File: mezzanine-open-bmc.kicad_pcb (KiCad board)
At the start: 2 copper layers, 85 x 54 mm, 64 parts, among them P1 CONN_02X20, P2 CONN_02X20, P3 CONN_01X04, P4 CONN_01X04, P5 CONN_01X04, SW1 PWR, SW2 RST, U1 FT230XS, U2 PMIC-CJT1117-3.3(SOT223), U3 DS3231N, U4 PCA9306, U5 M24C16-WMN6P, U6 REG_1.8V, U7 PCA9306, U8 PCA9306

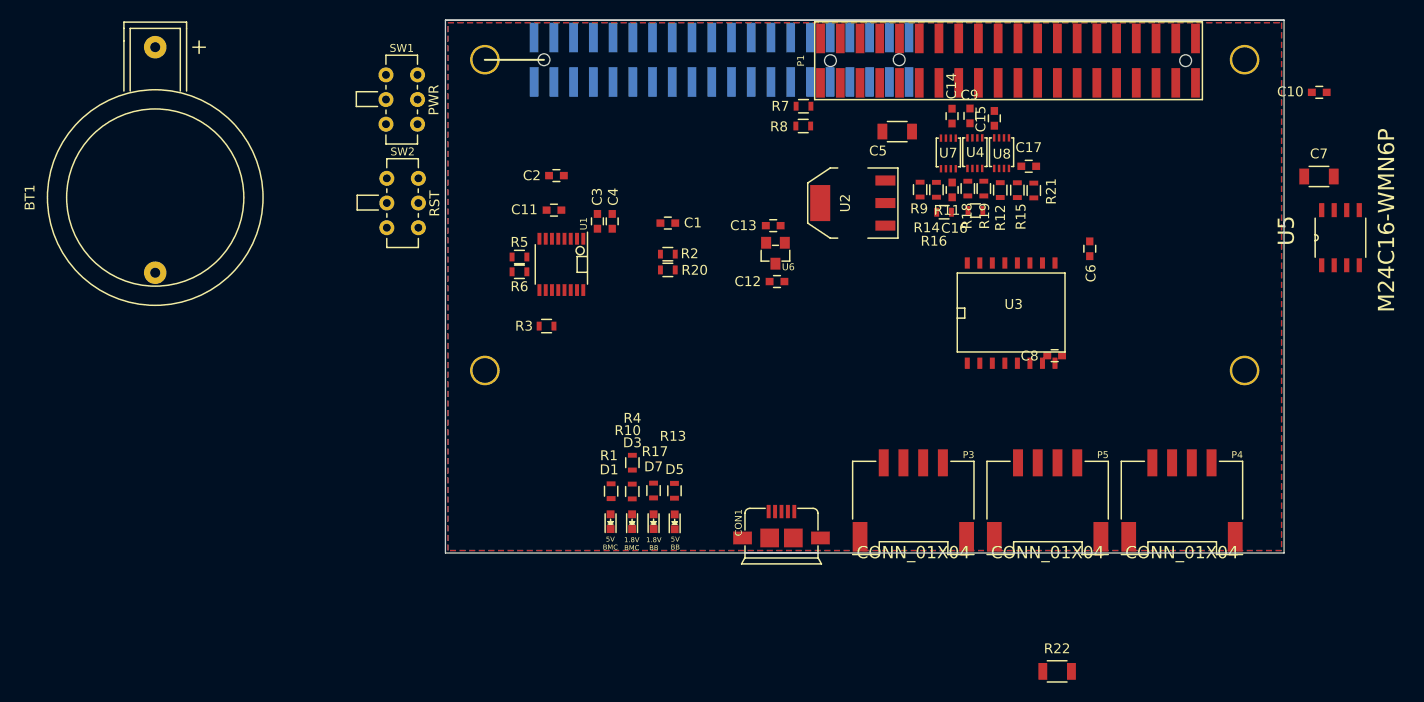
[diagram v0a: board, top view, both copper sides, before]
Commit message: Position USB and Connect
The USB is now positioned and all its important components are connected.

Signed-off-by: Sophie Haynes <sophie.haynes@linaro.org>
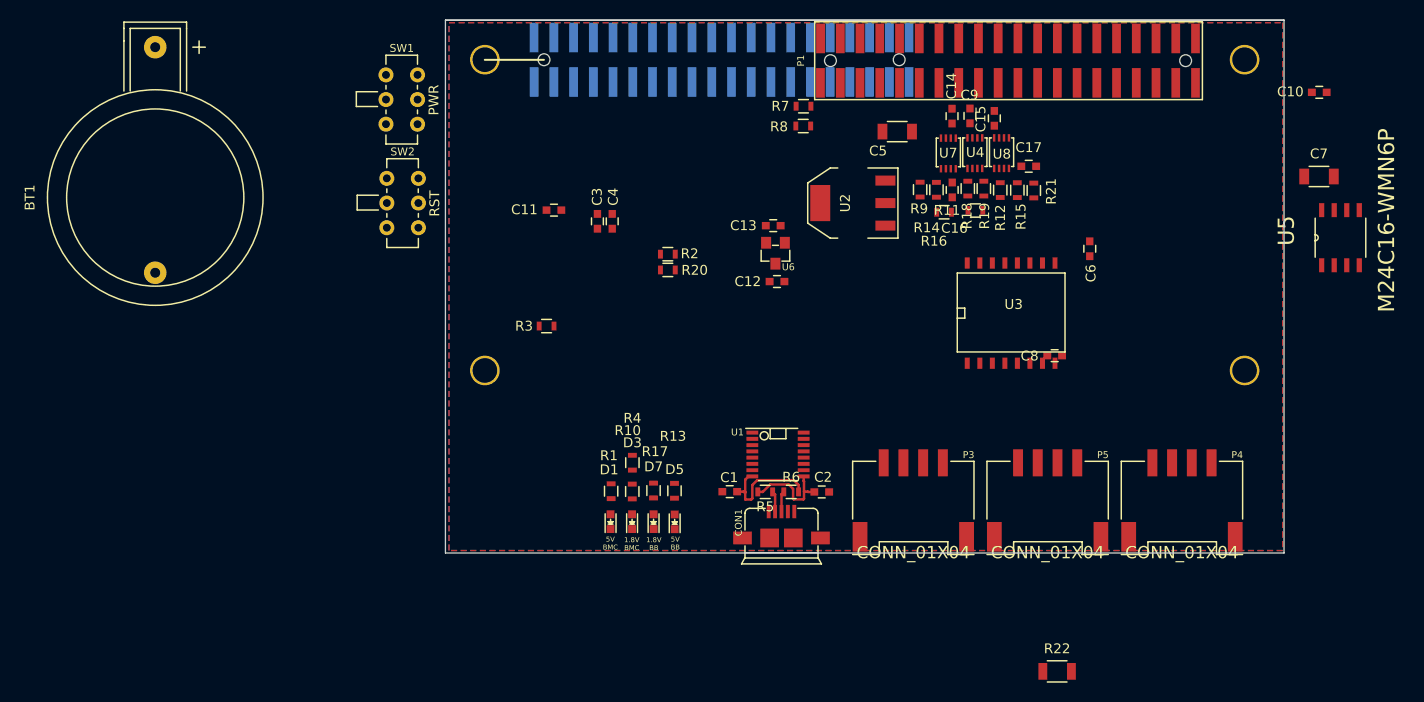
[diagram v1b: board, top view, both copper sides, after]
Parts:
- moved C2 41.8 mm to (138.1, 147.8)
- moved R6 35.4 mm to (135.0, 147.8), turned to 180 degrees
- moved R5 34.5 mm to (132.4, 147.8), turned to 0 degrees
- moved U1 29.2 mm to (133.7, 144.0), turned to 0 degrees
- moved C1 27.9 mm to (128.8, 147.8)
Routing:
- net /USB+: track 0.00 -> 13.7 mm
- net /USB-: track 0.00 -> 11.7 mm

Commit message: Move Switches to Bottom of Board
Signed-off-by: Sophie Haynes <sophie.haynes@linaro.org>
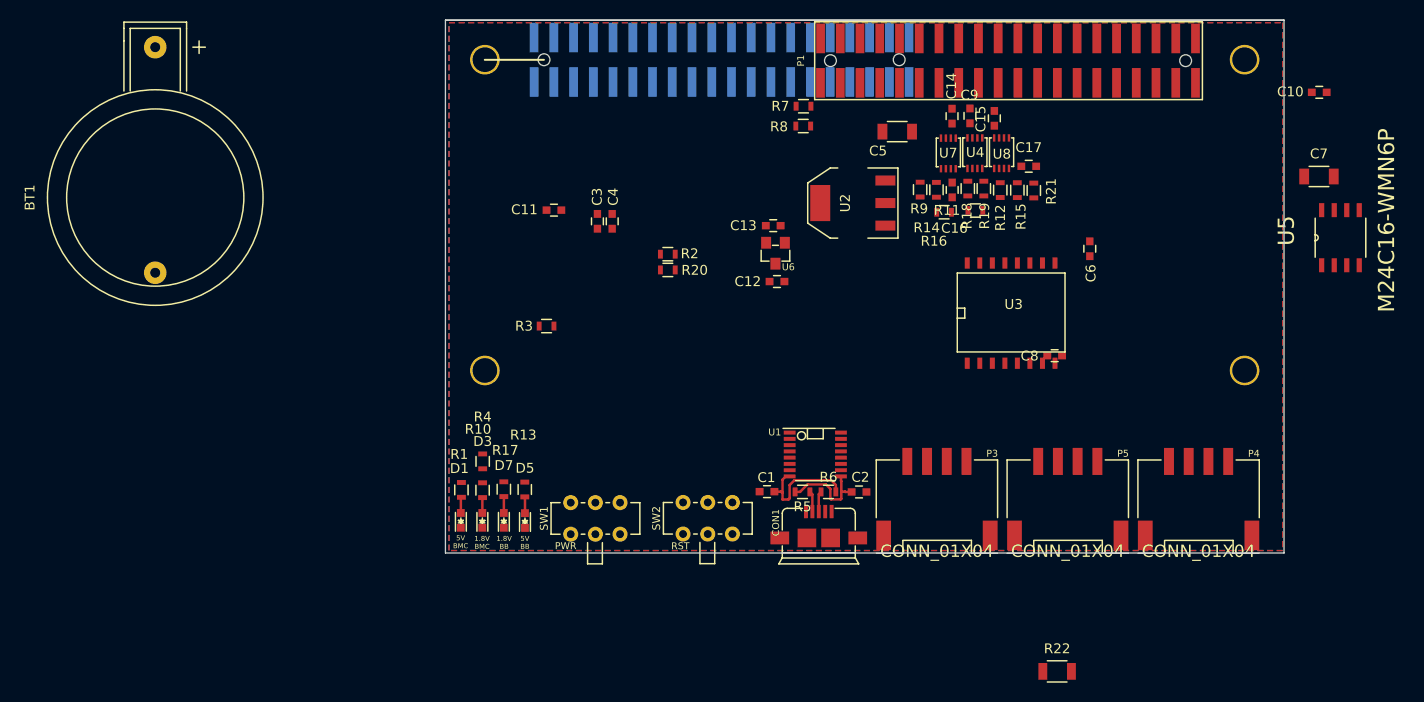
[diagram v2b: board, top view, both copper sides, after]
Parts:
- moved SW1 48.9 mm to (115.2, 152.1), turned to 0 degrees
- moved SW2 46.7 mm to (126.6, 152.1), turned to 0 degrees
- moved D3 15.2 mm to (103.7, 150.7)
- moved D7 15.2 mm to (105.9, 150.7)
- moved R13 15.2 mm to (108.0, 147.6)
- moved D1 15.2 mm to (101.6, 150.7)
- moved D5 15.2 mm to (108.1, 150.7)
- moved R1 15.2 mm to (101.6, 147.6)
- moved R10 15.2 mm to (103.8, 147.6)
- moved R17 15.2 mm to (105.9, 147.5)
- moved R4 15.2 mm to (103.8, 144.7)
- moved C1 3.78 mm to (132.6, 147.8)
- moved C2 3.78 mm to (141.9, 147.8)
- moved CON1 3.78 mm to (137.8, 154.0)
- moved R5 3.78 mm to (136.2, 147.8)
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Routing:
- net Net-(D7-Pad2): track 0.00 -> 1.66 mm
- net Net-(D5-Pad2): track 0.00 -> 1.65 mm
- net Net-(D1-Pad2): track 0.00 -> 1.61 mm
- net Net-(D3-Pad2): track 0.00 -> 1.57 mm

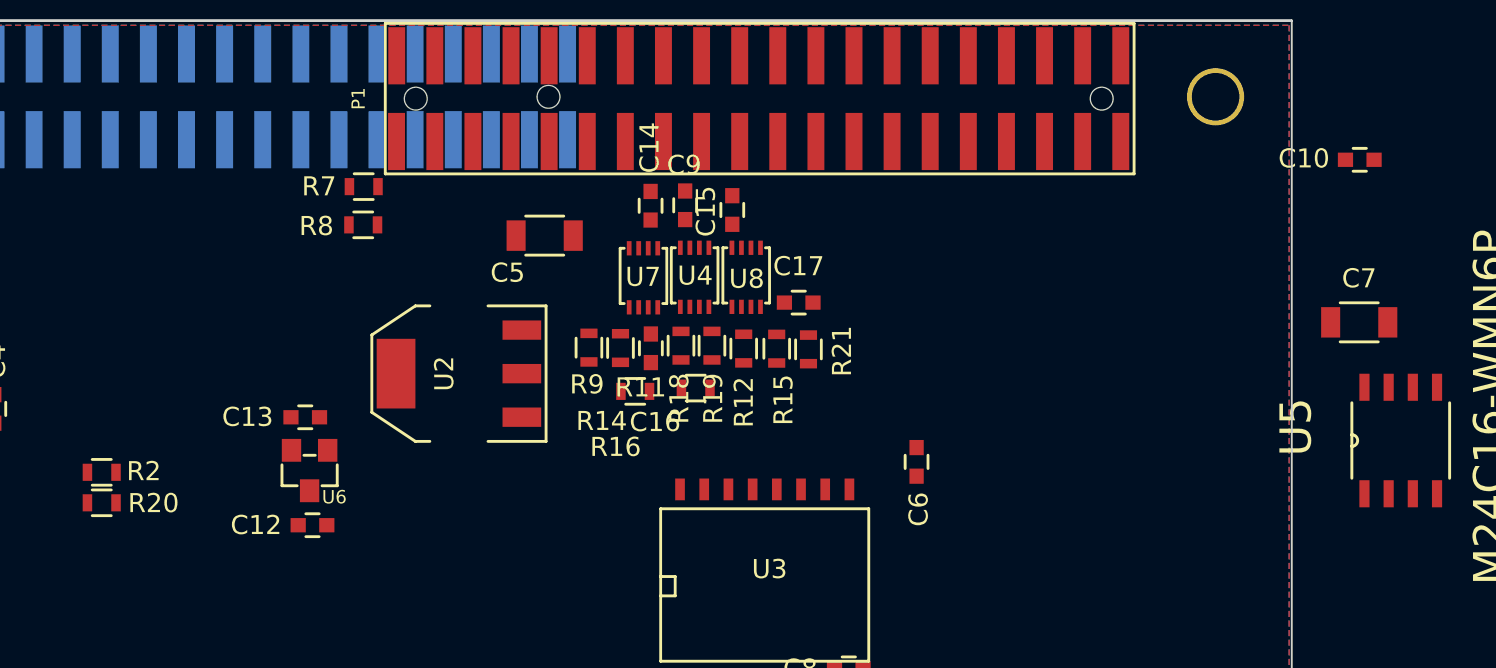
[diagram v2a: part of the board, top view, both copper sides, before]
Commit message: Position Grove Conn. Level Shifters
All three LS for the grove Connecotrs have been placed in a nice
layout in suitable location on board.

Signed-off-by: Sophie Haynes <sophie.haynes@linaro.org>
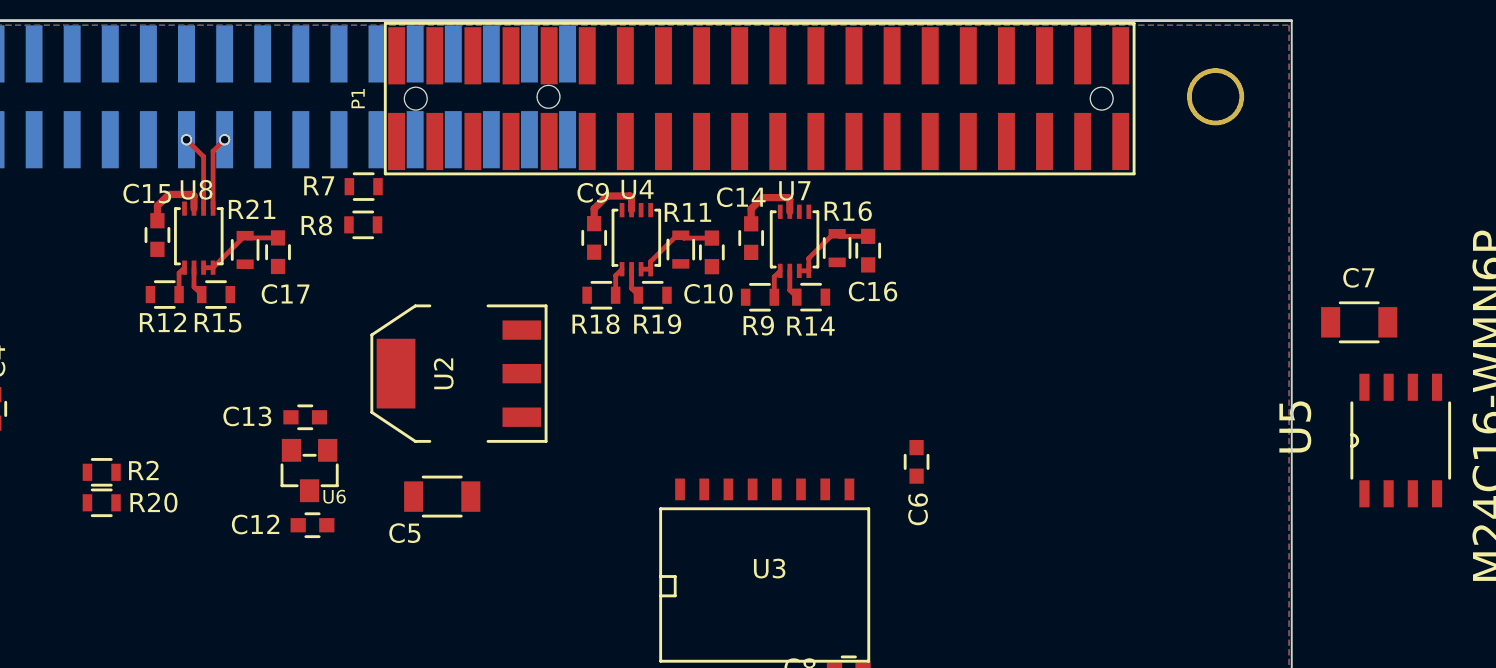
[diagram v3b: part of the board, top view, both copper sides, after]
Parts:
- moved C10 34.3 mm to (154.6, 112.2), turned to 270 degrees
- moved R12 30.5 mm to (125.9, 114.4), turned to 0 degrees
- moved C15 30.2 mm to (125.5, 111.3), turned to 270 degrees
- moved R21 30.0 mm to (130.1, 112.0)
- moved R15 29.6 mm to (128.5, 114.4), turned to 180 degrees
- moved U8 28.8 mm to (126.9, 109.9)
- moved C17 27.5 mm to (131.8, 112.2), turned to 270 degrees
- moved C5 14.7 mm to (140.4, 125.0)
- moved R16 13.0 mm to (161.1, 111.9), turned to 90 degrees
- moved C16 12.5 mm to (162.8, 112.1)
- moved R14 10.4 mm to (159.8, 114.5), turned to 180 degrees
- moved R9 9.36 mm to (157.1, 114.5), turned to 0 degrees
- moved U7 8.16 mm to (158.2, 110.0)
- moved R11 7.31 mm to (152.9, 112.0), turned to 90 degrees
- moved C14 5.54 mm to (156.6, 111.4), turned to 270 degrees
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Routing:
- net +1V8: track 0.00 -> 11.1 mm
- net Net-(C16-Pad1): track 0.00 -> 4.86 mm
- net Net-(C10-Pad1): track 0.00 -> 4.75 mm
- net Net-(C17-Pad1): track 0.00 -> 4.65 mm
- net I2C1_SDA: track 0.00 -> 4.06 mm, vias 0 -> 1
- net I2C1_SCL: track 0.00 -> 3.99 mm, vias 0 -> 1
- net I2C0_SCL_3.3: track 0.00 -> 1.72 mm
- net I2C1_SCL_3.3: track 0.00 -> 1.58 mm
- net I2C1_SCL_BMC_3.3: track 0.00 -> 1.53 mm
- net I2C1_SDA_3.3: track 0.00 -> 1.53 mm
- net I2C1_SDA_BMC_3.3: track 0.00 -> 1.52 mm
- net I2C0_SDA_3.3: track 0.00 -> 1.50 mm

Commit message: [WIP] PCB In Progress
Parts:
- U2: value PMIC-CJT1117-3.3(SOT223) -> SOT223
- moved R22 56.2 mm to (166.2, 110.0), turned to 180 degrees
- moved BT1 41.1 mm to (111.7, 119.5), turned to 270 degrees
- moved C11 38.0 mm to (142.4, 140.6), turned to 0 degrees
- moved C3 35.8 mm to (142.4, 143.8), turned to 0 degrees
- moved C5 34.5 mm to (171.5, 109.9)
- moved U3 33.8 mm to (123.8, 134.5), turned to 90 degrees
- moved C4 33.6 mm to (142.4, 142.3), turned to 0 degrees
- moved C8 31.2 mm to (130.7, 137.0), turned to 90 degrees
- moved U5 29.8 mm to (164.5, 136.3), turned to 0 degrees
- moved C7 27.3 mm to (165.8, 130.9), turned to 180 degrees
- moved U2 26.6 mm to (167.3, 124.0), turned to 0 degrees
- moved R3 25.1 mm to (132.5, 142.8)
- moved P4 25.0 mm to (151.3, 144.8)
- moved R2 24.5 mm to (132.4, 146.1), turned to 0 degrees
- moved R20 21.6 mm to (132.5, 144.5), turned to 0 degrees
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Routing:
- net +3V3: track 0.00 -> 96.0 mm
- net UART1_TX_BMC: track 0.00 -> 50.9 mm
- net UART1_RX_BMC: track 0.00 -> 48.0 mm
- net +1V8: track 11.1 -> 58.4 mm, vias 0 -> 2
- net GPIO_A: track 0.00 -> 41.9 mm, vias 0 -> 1
- net I2C0_SCL: track 0.00 -> 41.6 mm, vias 0 -> 1
- net I2C0_SDA: track 0.00 -> 40.1 mm, vias 0 -> 1
- net I2C1_SCL_BMC_3.3: track 1.53 -> 41.2 mm, vias 0 -> 2
- net I2C0_SDA_3.3: track 1.50 -> 40.7 mm, vias 0 -> 2
- net I2C1_SDA_BMC_3.3: track 1.52 -> 40.4 mm, vias 0 -> 2
- net I2C0_SCL_3.3: track 1.72 -> 40.5 mm, vias 0 -> 2
- net GPIO_B: track 0.00 -> 38.4 mm, vias 0 -> 1
- net GPIO_C_BMC: track 0.00 -> 37.4 mm, vias 0 -> 2
- net +5V: track 0.00 -> 35.3 mm
- net PWR_BTN_N: track 0.00 -> 30.5 mm, vias 0 -> 1
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
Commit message: [WIP]
Updating the repository, still drawing traces.

Signed-off-by: Sophie Haynes <sophie.haynes@linaro.org>
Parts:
- moved R22 9.64 mm to (160.6, 117.8)
- moved C5 3.03 mm to (174.4, 109.5), turned to 0 degrees
- moved R12 2.47 mm to (128.5, 116.1), turned to 180 degrees
- moved C10 2.08 mm to (155.1, 114.2)
- moved R11 2.08 mm to (153.5, 114.0)
- moved C17 2.06 mm to (132.4, 114.1)
- moved R21 2.06 mm to (130.6, 114.0)
- moved C9 2.01 mm to (147.8, 109.5), turned to 180 degrees
- moved R16 1.97 mm to (161.8, 113.8)
- moved C16 1.97 mm to (163.4, 113.9)
- moved R15 1.67 mm to (128.4, 114.5)
- moved C6 1.57 mm to (173.8, 112.0), turned to 0 degrees
- moved C14 1.57 mm to (156.6, 109.8)
- moved R7 0.96 mm to (135.0, 109.3)
- moved R8 0.96 mm to (137.1, 109.4)
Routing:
- net +1V8: track 58.4 -> 121.5 mm, vias 2 -> 0
- net +5V: track 35.3 -> 94.7 mm, vias 0 -> 2
- net UART1_TX_BMC: track 50.9 -> 1.40 mm
- net I2C0_SCL_3.3: track 40.5 -> 89.9 mm, vias 2 -> 3
- net I2C1_SCL_3.3: track 0.16 -> 45.9 mm
- net I2C1_SDA_3.3: track 0.25 -> 44.4 mm
- net I2C0_SDA_3.3: track 40.7 -> 84.1 mm, vias 2 -> 3
- net I2C0_SDA: track 40.1 -> 9.24 mm, vias 1 -> 0
- net +3V3: track 96.0 -> 125.1 mm
- net UART1_TX: track 17.6 -> 39.4 mm, vias 0 -> 1
- net SYS_DCIN: track 2.00 -> 22.5 mm, vias 0 -> 2
- net UART1_RX: track 15.0 -> 33.5 mm, vias 0 -> 1
- net SYS_DCIN_BMC: track 14.8 -> 21.8 mm
- net GPIO_D_BMC: track 28.0 -> 31.6 mm, vias 1 -> 2
- net GND: track 3.21 -> 0.05 mm
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
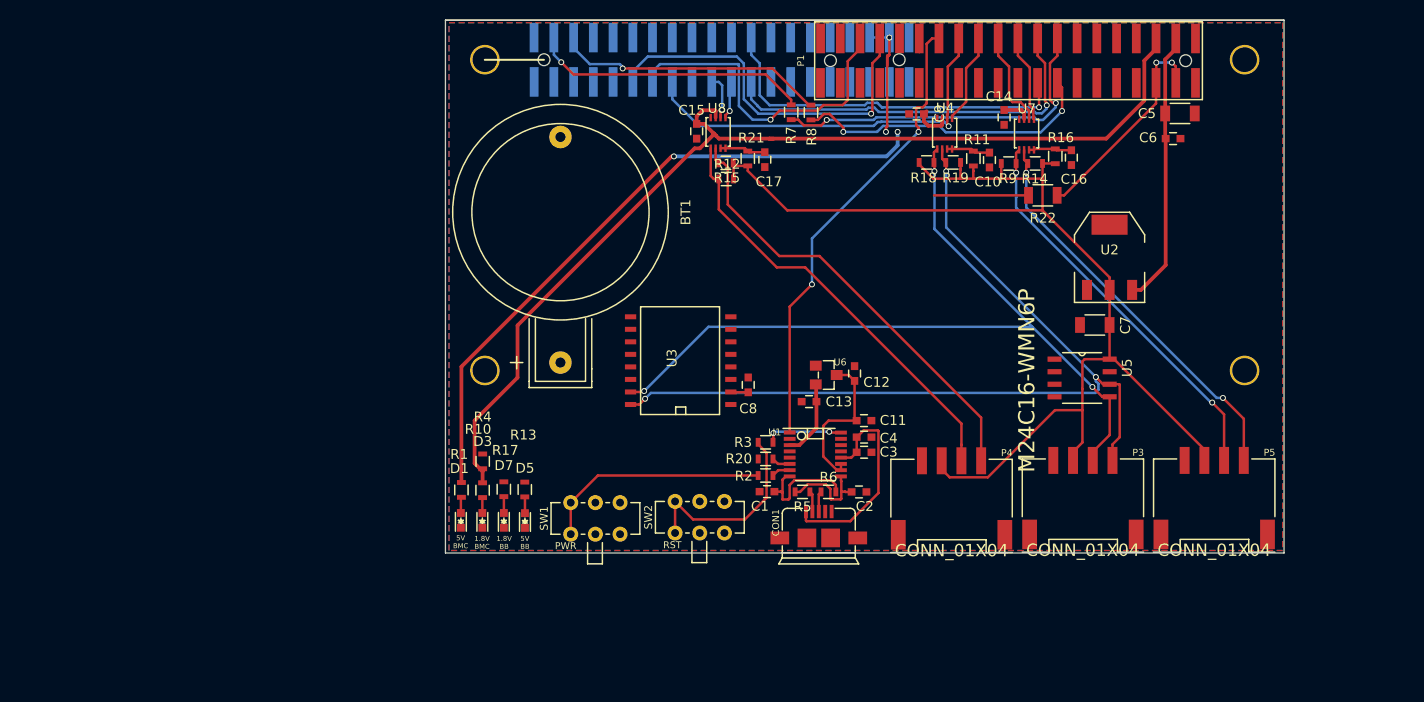
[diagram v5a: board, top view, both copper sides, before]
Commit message: [WIP] Just several GPIO require connecting
Most components are connected now. I dislike the bunching of traces, and some
1v8 lines are quite long which is bad for interference.

The bunching of all the traces so close to the pins is causing issues getting
the last connectors connected. I may have to move the regulators down,
and move all the traces down too. :(

Signed-off-by: Sophie Haynes <s.c.haynes@rgu.ac.uk>
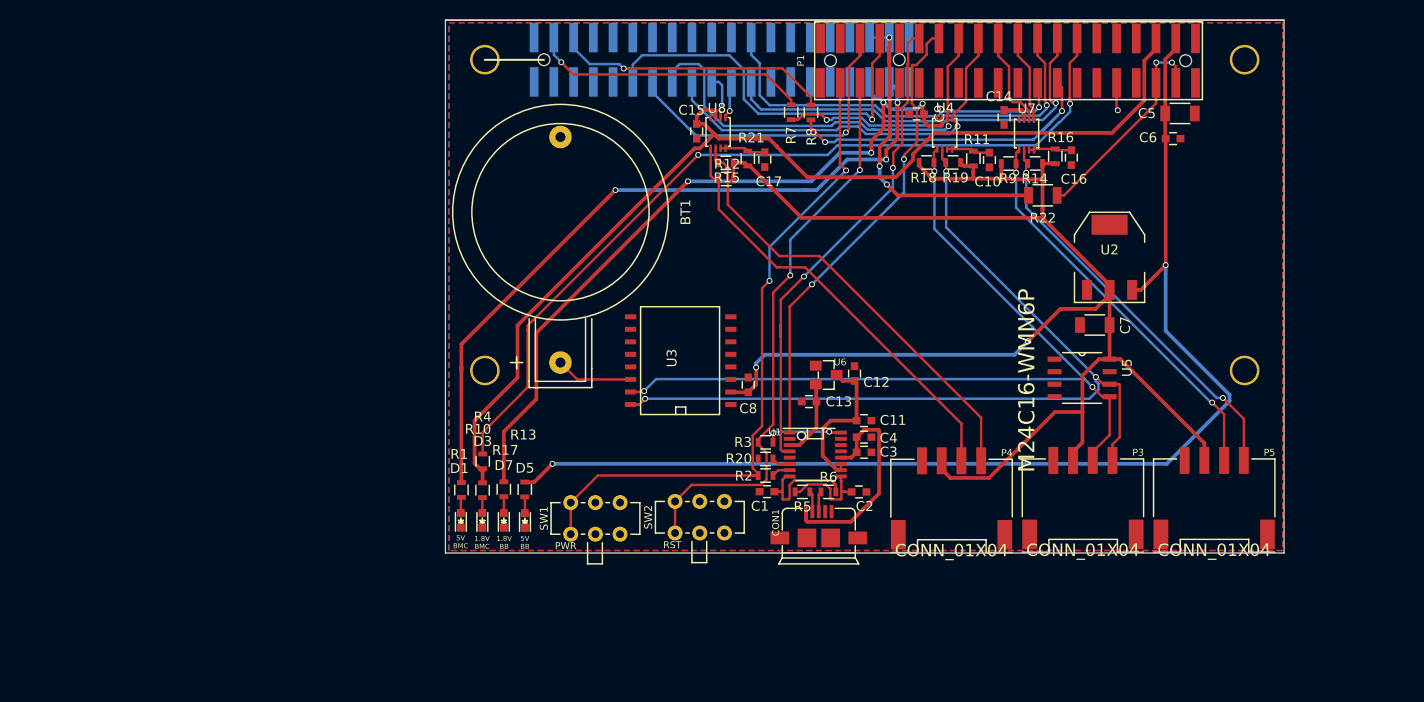
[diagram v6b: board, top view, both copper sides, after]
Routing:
- net +5V: track 94.7 -> 193.3 mm, vias 2 -> 5
- net GPIO_E_BMC: track 0.00 -> 86.8 mm, vias 0 -> 2
- net +1V8: track 121.5 -> 195.9 mm, vias 0 -> 4
- net UART1_TX_BMC: track 1.40 -> 51.4 mm, vias 0 -> 2
- net PWR_BTN_BMC: track 23.3 -> 68.3 mm, vias 0 -> 2
- net +3V3: track 125.1 -> 167.5 mm, vias 0 -> 2
- net RST_BTN_BMC: track 20.1 -> 58.2 mm, vias 0 -> 2
- net I2C0_SDA: track 9.24 -> 41.1 mm, vias 0 -> 1
- net SYS_DCIN: track 22.5 -> 34.2 mm, vias 2 -> 3
- net Net-(BT1-Pad1): track 0.00 -> 7.82 mm
- net GPIO_D_BMC: track 31.6 -> 35.9 mm
- net GPIO_J: track 0.00 -> 3.89 mm, vias 0 -> 1
- net I2C0_SCL: track 42.8 -> 46.5 mm
- net I2C0_SDA_3.3: track 84.1 -> 87.2 mm
- net UART1_RX: track 33.5 -> 36.2 mm
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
